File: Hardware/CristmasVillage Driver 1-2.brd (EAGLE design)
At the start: 94.2 x 42.9 mm, 54 parts, among them CN1 MJ-180SMT, CN2-PROG JST-6PSPI-SIDE-S6B, CN3-SERIAL JST-4PSIDE-S4B, CN5-LEDSTRIPS HDR_2X10_SIDE-MOUNT, IC1 UA78M05DCY, IC2 LM358D, IC3 LM358D, IC4 LM358D, IC5 ATTINY-4/5/9/10, IC6 TINY2313-*S*, Q1 Si2309CD, Q10 NX7002AKW, Q11 NX7002AKW, Q12 NX7002AKW, Q2 NX7002AKW, Q3 NX7002AKW, Q4 NX7002AKW, Q5 NX7002AKW, Q6 NX7002AKW, Q7 NX7002AKW, Q8 NX7002AKW, Q9 NX7002AKW, SW1 POWER, SW2 NIGHT-MODE

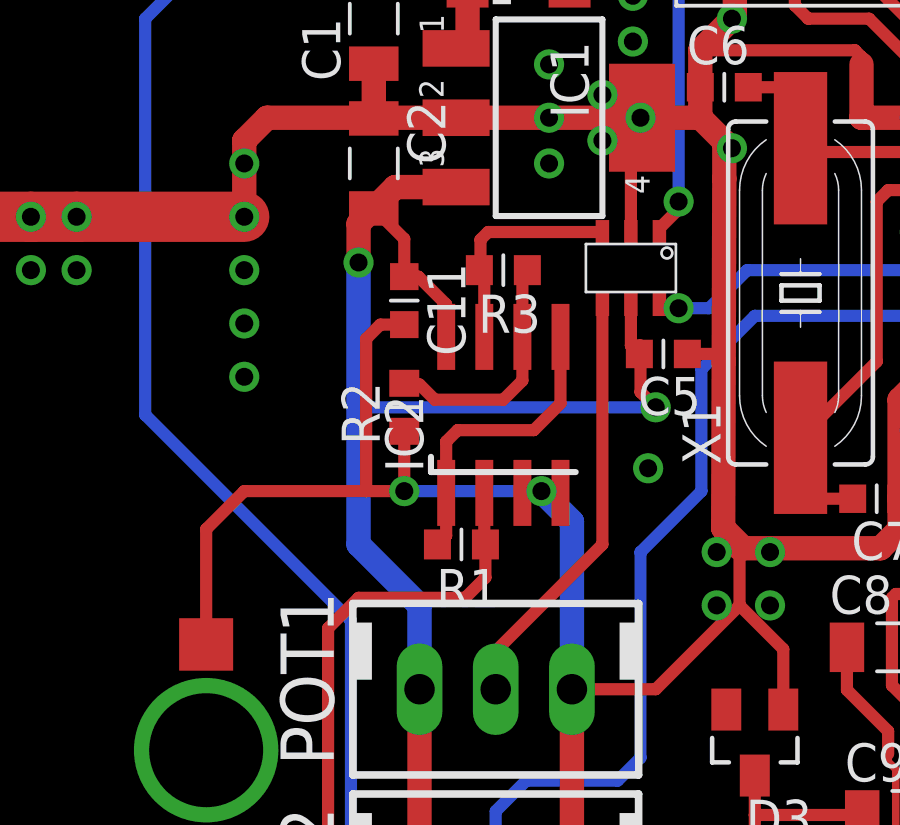
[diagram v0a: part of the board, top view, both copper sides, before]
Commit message: Added opt. filter caps to hardware & created PDF exports of v1.2
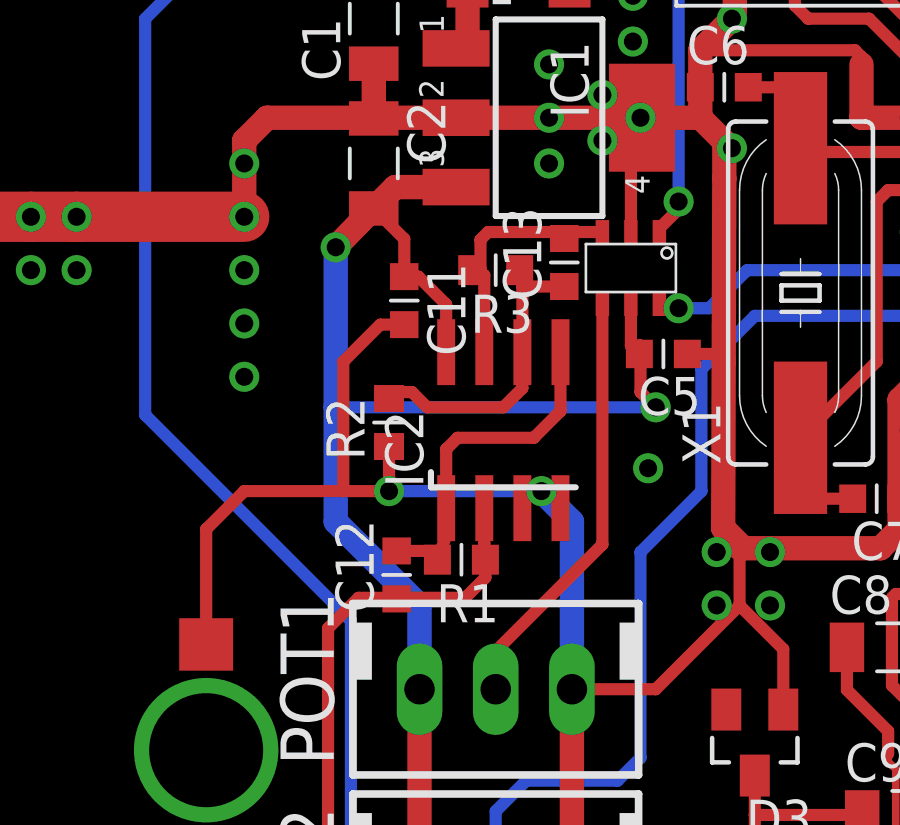
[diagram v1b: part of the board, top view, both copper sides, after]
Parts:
- added C12: 560pF, ipc-7351-capacitor:CAPC1608X92N
- added C13: 56nF, ipc-7351-capacitor:CAPC1608X92N
- R1: value 1M -> 10M
- R3: value 490k -> 100k
- moved R2 0.72 mm to (99.3, 48.5)
- moved IC2 0.51 mm to (103.1, 48.3)
- moved R1 0.51 mm to (101.7, 43.9)
- moved R3 0.25 mm to (102.9, 53.6)
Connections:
- net N$2: now also C12.1
- net N$3: now also C12.2
- net N$6: now also C13.1
- net N$7: now also C13.2
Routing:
- net N$6: track 8.18 -> 10.3 mm
- net V+: track 148.5 -> 150.4 mm
- net N$3: track 10.1 -> 11.7 mm
- net N$7: track 7.50 -> 8.93 mm
- net GND: track 277.0 -> 277.7 mm
